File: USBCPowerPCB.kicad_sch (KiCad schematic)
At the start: 36 parts, among them J1 UJ31-CH-31N-SMT-TR, J10 GND_BANANA_OUT, J11 12V_BANANA_IN, J12 GND_BANANA_IN, J2 CC, J3 12V_OUT, J4 5V_ISOOUT, J5 5V_UNISOOUT, J6 12V_OUT_PIN, J7 5V_ISOOUT_PIN, J8 5V_UNISOOUT_PIN, J9 12V_BANANA_OUT, U1 TVS2200DRV

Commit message: intermediate progress push before addressing Champers' and Lakshay's review comments
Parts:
- removed J1: UJ31-CH-31N-SMT-TR, UTSVT_Connectors:CUI_UJ31-CH-31N-SMT-TR, symbol utsvt-connectors:UJ31-CH-31N-SMT-TR
- removed J11: 12V_BANANA_IN, UTSVT_Connectors:Banana_Jack_Horizontal, symbol Connector_Generic:Conn_01x01
- removed J12: GND_BANANA_IN, UTSVT_Connectors:Banana_Jack_Horizontal, symbol Connector_Generic:Conn_01x01
- added C2: 3.3uF, Capacitor_SMD:C_0805_2012Metric, symbol Device:C_Small
- added H1, H2, H3, H4: M3, MountingHole:MountingHole_3.2mm_M3, symbol Mechanical:MountingHole
- added J1: USB_C_Receptacle_PowerOnly_6P, UTSVT_Connectors:TYPEC31M17, symbol Connector:USB_C_Receptacle_PowerOnly_6P
- C1: symbol Device:C -> Device:C_Small
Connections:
- net CC1: now also J1.A5 (CC1)
- net CC2: now also J1.B5 (CC2)
- net GND: now also C2.2, J1.A12 (GND), J1.B12 (GND)
- net VBUS_USBIN: now also C2.1, J1.A9 (VBUS), J1.B9 (VBUS)
- no-connect marks 15 -> 1
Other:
- note added: "Mounting Holes"
- moved on the sheet: C1, J10, J2, J9, TP1, TP2, TP3, TP4, TP5, TP6, TP7, TP8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

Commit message: Added ideal diode controller & mosfet for 12V buck power protection
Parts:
- J1: Manufacturer_Name (none) -> Korean Hroparts Elec; Mouser Part Number (none) -> TYPE-C-31-M-17
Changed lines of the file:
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@@
 		(on_board yes)
 		(dnp no)
-		(property "Reference" "#PWR026"
+		(property "Reference" "#PWR027"
 			(at 224.79 74.93 0)
 			(effects
@@
 			(project "USBCPowerPCB"
 				(path "/f58400c5-df4b-4929-8d2b-33c0fe23fcd9"
-					(reference "#PWR026")
+					(reference "#PWR027")
 					(unit 1)
 				)
@@
 		(on_board yes)
 		(dnp no)
-		(property "Reference" "#PWR024"
+		(property "Reference" "#PWR025"
 			(at 224.79 53.34 0)
 			(effects
@@
 			(project "USBCPowerPCB"
 				(path "/f58400c5-df4b-4929-8d2b-33c0fe23fcd9"
-					(reference "#PWR024")
+					(reference "#PWR025")
 					(unit 1)
 				)
@@
 		(on_board yes)
 		(dnp no)
-		(property "Reference" "#PWR025"
+		(property "Reference" "#PWR026"
 			(at 224.79 64.77 0)
 			(effects
@@
 			(project "USBCPowerPCB"
 				(path "/f58400c5-df4b-4929-8d2b-33c0fe23fcd9"
-					(reference "#PWR025")
+					(reference "#PWR026")
 					(unit 1)
 				)
@@
 		(dnp no)
 		(fields_autoplaced yes)
-		(property "Reference" "#PWR028"
+		(property "Reference" "#PWR023"
 			(at 220.98 161.29 0)
 			(effects
@@
 			(project ""
 				(path "/f58400c5-df4b-4929-8d2b-33c0fe23fcd9"
-					(reference "#PWR028")
+					(reference "#PWR023")
 					(unit 1)
 				)
@@
 		(dnp no)
 		(fields_autoplaced yes)
-		(property "Reference" "#PWR023"
+		(property "Reference" "#PWR024"
 			(at 224.79 46.99 0)
 			(effects
@@
 			(project "USBCPowerPCB"
 				(path "/f58400c5-df4b-4929-8d2b-33c0fe23fcd9"
-					(reference "#PWR023")
+					(reference "#PWR024")
 					(unit 1)
 				)
@@
 			)
 		)
+		(property "Manufacturer_Name" "Korean Hroparts Elec"
+			(at 33.02 106.68 0)
+			(effects
+				(font
+					(size 1.27 1.27)
+				)
+				(hide yes)
+			)
+		)
+		(property "Mouser Part Number" " TYPE-C-31-M-17"
+			(at 33.02 106.68 0)
+			(effects
+				(font
+					(size 1.27 1.27)
+				)
+				(hide yes)
+			)
+		)
 		(pin "B9"
 		)
@@
 		(on_board yes)
 		(dnp no)
-		(property "Reference" "#PWR027"
+		(property "Reference" "#PWR028"
 			(at 224.79 81.28 0)
 			(effects
@@
 			(project "USBCPowerPCB"
 				(path "/f58400c5-df4b-4929-8d2b-33c0fe23fcd9"
-					(reference "#PWR027")
+					(reference "#PWR028")
 					(unit 1)
 				)

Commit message: started routing
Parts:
- J4: symbol Connector_Generic:Conn_01x02 -> Connector_Generic:Conn_01x04
- TP1, TP2, TP3, TP4, TP5, TP6, TP7, TP8, TP9: footprint TestPoint:TestPoint_Pad_D2.5mm -> TestPoint:TestPoint_Plated_Hole_D3.0mm
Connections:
- net GNDPWR: now also J4.4 (Pin_4); no longer J4.2 (Pin_2)
- no-connect marks 1 -> 3
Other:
- moved on the sheet: D2, D3, D4, D5, D6, D7, J2, J3, J6, J7, J8, R1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

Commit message: redid cypd layout, halfway through 12v buck layout
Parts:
- J4: footprint UTSVT_Connectors:Molex_MicroFit3.0_1x2xP3.00mm_PolarizingPeg_Vertical -> UTSVT_Connectors:Molex_MicroFit3.0_1x4xP3.00mm_PolarizingPeg_Vertical
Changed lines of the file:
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@@
 			)
 		)
-		(property "Footprint" "UTSVT_Connectors:Molex_MicroFit3.0_1x2xP3.00mm_PolarizingPeg_Vertical"
+		(property "Footprint" "UTSVT_Connectors:Molex_MicroFit3.0_1x4xP3.00mm_PolarizingPeg_Vertical"
 			(at 207.01 55.88 0)
 			(effects

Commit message: big component layout moment
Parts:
- TP1, TP2, TP3, TP4, TP5, TP6, TP7, TP8, TP9: footprint TestPoint:TestPoint_Plated_Hole_D3.0mm -> TestPoint:TestPoint_Plated_Hole_D2.0mm
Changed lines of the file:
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@@
 			)
 		)
-		(property "Footprint" "TestPoint:TestPoint_Plated_Hole_D3.0mm"
+		(property "Footprint" "TestPoint:TestPoint_Plated_Hole_D2.0mm"
 			(at 194.31 139.7 0)
 			(effects
@@
 			)
 		)
-		(property "Footprint" "TestPoint:TestPoint_Plated_Hole_D3.0mm"
+		(property "Footprint" "TestPoint:TestPoint_Plated_Hole_D2.0mm"
 			(at 215.9 140.97 0)
 			(effects
@@
 			)
 		)
-		(property "Footprint" "TestPoint:TestPoint_Plated_Hole_D3.0mm"
+		(property "Footprint" "TestPoint:TestPoint_Plated_Hole_D2.0mm"
 			(at 215.9 132.08 0)
 			(effects
@@
 			)
 		)
-		(property "Footprint" "TestPoint:TestPoint_Plated_Hole_D3.0mm"
+		(property "Footprint" "TestPoint:TestPoint_Plated_Hole_D2.0mm"
 			(at 231.14 137.16 0)
 			(effects
@@
 			)
 		)
-		(property "Footprint" "TestPoint:TestPoint_Plated_Hole_D3.0mm"
+		(property "Footprint" "TestPoint:TestPoint_Plated_Hole_D2.0mm"
 			(at 194.31 132.08 0)
 			(effects
@@
 			)
 		)
-		(property "Footprint" "TestPoint:TestPoint_Plated_Hole_D3.0mm"
+		(property "Footprint" "TestPoint:TestPoint_Plated_Hole_D2.0mm"
 			(at 228.6 154.94 0)
 			(effects
@@
 			)
 		)
-		(property "Footprint" "TestPoint:TestPoint_Plated_Hole_D3.0mm"
+		(property "Footprint" "TestPoint:TestPoint_Plated_Hole_D2.0mm"
 			(at 190.5 154.94 0)
 			(effects
@@
 			)
 		)
-		(property "Footprint" "TestPoint:TestPoint_Plated_Hole_D3.0mm"
+		(property "Footprint" "TestPoint:TestPoint_Plated_Hole_D2.0mm"
 			(at 172.72 154.94 0)
 			(effects
@@
 			)
 		)
-		(property "Footprint" "TestPoint:TestPoint_Plated_Hole_D3.0mm"
+		(property "Footprint" "TestPoint:TestPoint_Plated_Hole_D2.0mm"
 			(at 215.9 154.94 0)
 			(effects

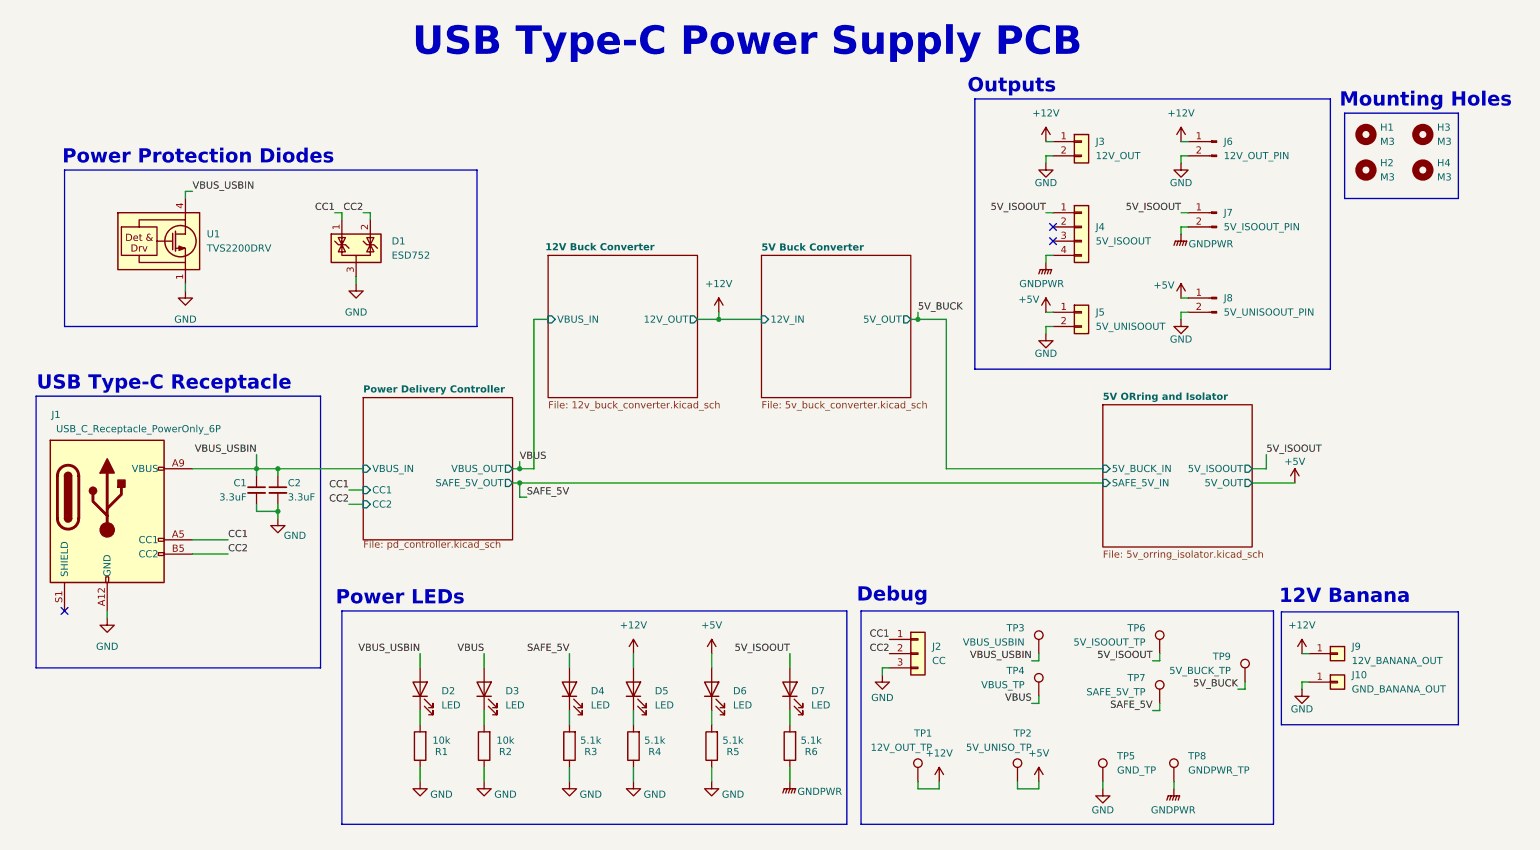
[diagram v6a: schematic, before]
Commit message: added testpoints everywhere :)
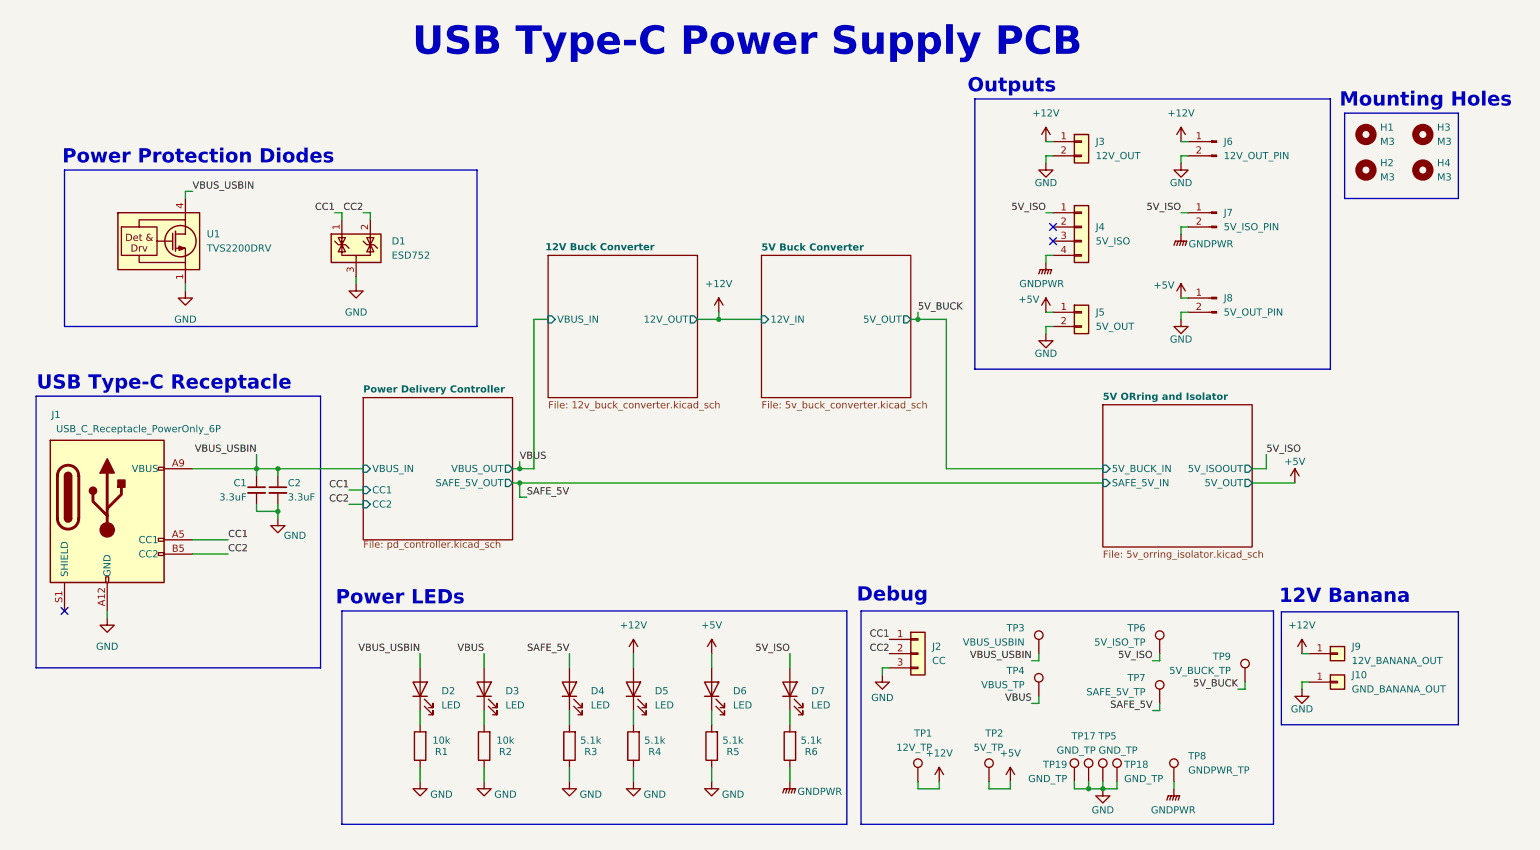
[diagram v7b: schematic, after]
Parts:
- added TP17, TP18: GND_TP, TestPoint:TestPoint_THTPad_1.0x1.0mm_Drill0.5mm, symbol Connector:TestPoint
- added TP19: GND_TP, TestPoint:TestPoint_Plated_Hole_D2.0mm, symbol Connector:TestPoint
- J4: value 5V_ISOOUT -> 5V_ISO
- J5: value 5V_UNISOOUT -> 5V_OUT
- J7: value 5V_ISOOUT_PIN -> 5V_ISO_PIN
- J8: value 5V_UNISOOUT_PIN -> 5V_OUT_PIN
- TP1: value 12V_OUT_TP -> 12V_TP
- TP2: value 5V_UNISO_TP -> 5V_TP
- TP5: footprint TestPoint:TestPoint_Plated_Hole_D2.0mm -> TestPoint:TestPoint_THTPad_1.0x1.0mm_Drill0.5mm
- TP6: value 5V_ISOOUT_TP -> 5V_ISO_TP
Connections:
- net GND: now also TP17.1, TP18.1, TP19.1
- net 5V_ISOOUT renamed 5V_ISO
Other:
- moved on the sheet: TP2

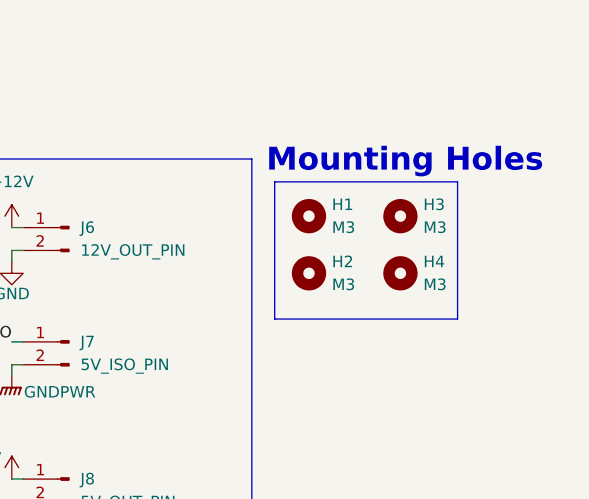
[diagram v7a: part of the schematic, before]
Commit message: cleared most DRC errors, need to fix DRC warnings
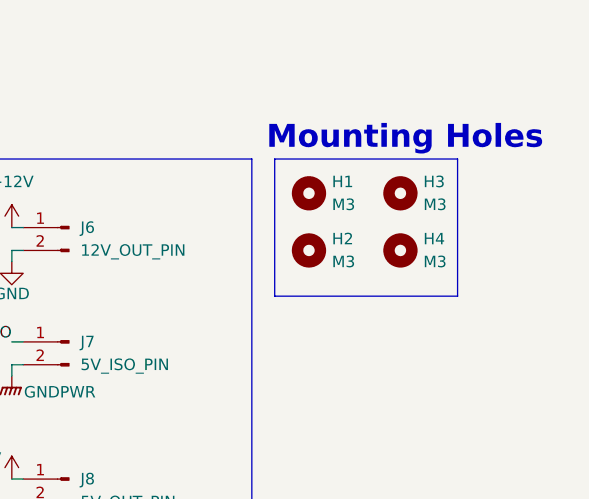
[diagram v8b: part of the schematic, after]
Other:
- moved on the sheet: H1, H2, H3, H4
